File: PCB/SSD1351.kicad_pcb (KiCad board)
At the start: 2 copper layers, 38 x 41.1 mm, 20 parts, among them J1 Conn_01x07

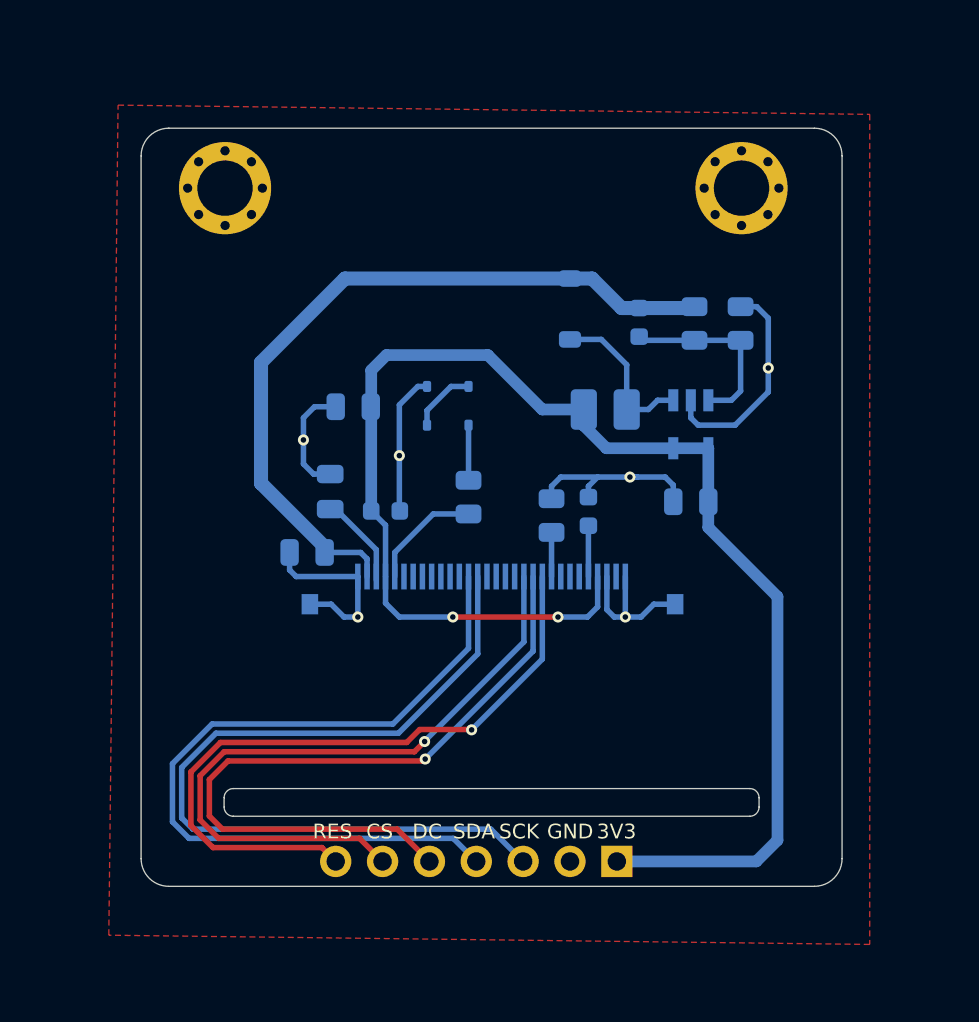
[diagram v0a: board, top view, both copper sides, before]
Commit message: Updated PCB
Consulted datasheets and adjusted cap ratings.
Reworked power distribution and location.
Started tracking down specific components and updating the BOM.
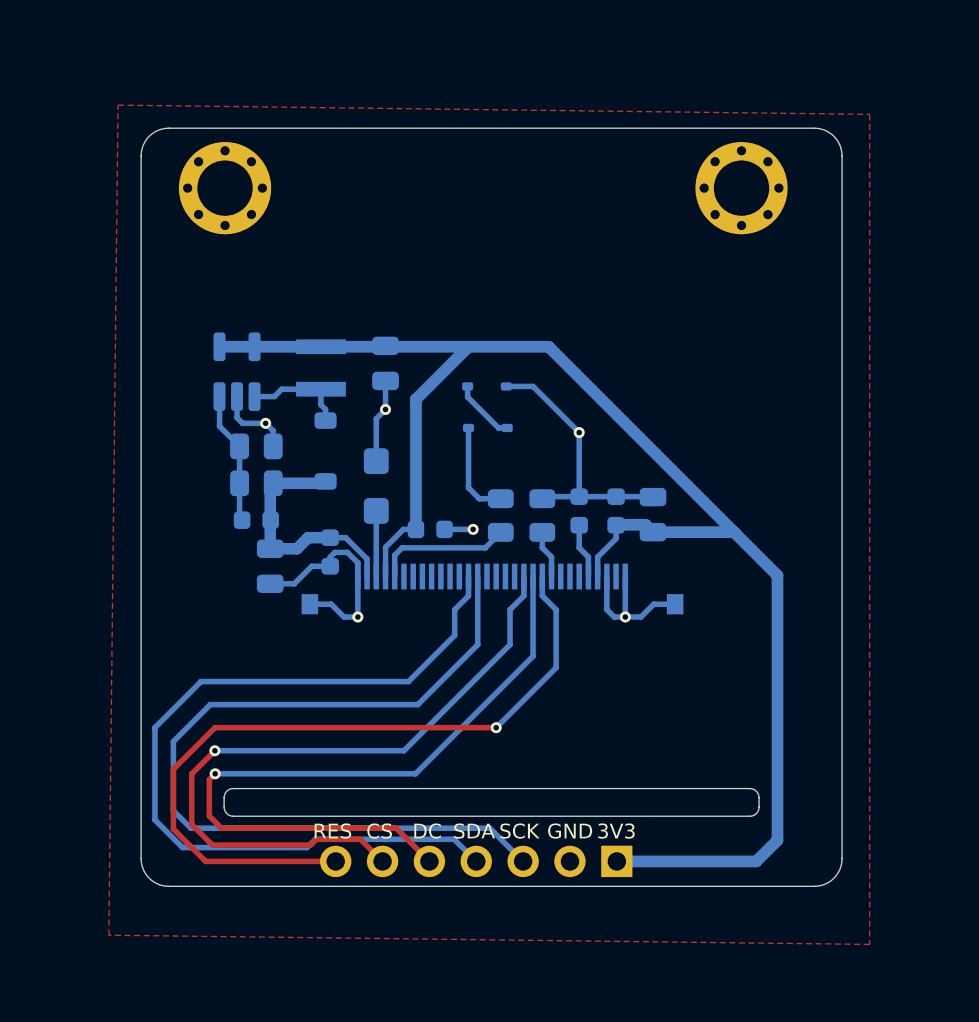
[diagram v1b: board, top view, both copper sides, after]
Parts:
- added C8: 0.1uF, Capacitor_SMD:C_0603_1608Metric, B.Cu at (128.2, 56.8)
- added C9: 0.1uF, Capacitor_SMD:C_0603_1608Metric, B.Cu at (112.8, 59.0)
- C1: value 10uf -> 10uF
- C2: value 10uF -> 4.7uF 25v Tantalum; footprint Capacitor_SMD:C_0805_2012Metric -> Capacitor_Tantalum_SMD:CP_EIA-3216-18_Kemet-A
- C5, C7: value 10uF -> 4.7uF
- C6: value 0.1uF -> 140pF
- D1, D2: value 1N4148 -> 1N4148 0.5W
- L1: value 10uH -> LVS303012H-100M-N; footprint Inductor_SMD:L_1008_2520Metric_Pad1.43x2.20mm_HandSolder -> Inductor_SMD:L_Sunlord_SWPA3012S
- R1: value 50 -> 50 1/4W
- R2: value 600K -> 560K
- R3: value 100K -> 137K
- R4: value 10K -> 14.3K
- U1: value ~ -> SFV30R-4STBE1HLF
- U2: value ~ -> FAN5331SXCT-ND; footprint SSD1351:SOT23-5 -> Package_TO_SOT_SMD:SOT-23-5_HandSoldering
- moved R4 27.1 mm to (108.8, 53.2), turned to 180 degrees
- moved R3 25.3 mm to (108.8, 55.2), turned to 0 degrees
- moved U2 24.8 mm to (107.7, 49.2), turned to 90 degrees
- moved C6 23.4 mm to (108.8, 57.2), turned to 180 degrees
- moved C7 18.2 mm to (115.8, 48.8), turned to -90 degrees
- moved C5 17.3 mm to (130.2, 57.0), turned to 90 degrees
- moved L1 15.6 mm to (112.2, 49.0), turned to -90 degrees
- moved D3 15.3 mm to (112.5, 53.5), turned to 90 degrees
- moved D2 3.42 mm to (121.2, 50.0), turned to 180 degrees
- moved C3 2.62 mm to (118.2, 57.8)
- moved C2 2.52 mm to (115.2, 55.4)
- moved C1 2.14 mm to (109.5, 59.8), turned to 90 degrees
- moved R1 2.02 mm to (122.0, 57.0)
- moved D1 1.59 mm to (121.3, 52.2), turned to 180 degrees
- moved C4 0.50 mm to (126.2, 56.8)
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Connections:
- C1 pad 1: /+13V -> GND
- C1 pad 2: GND -> /+13V
- REF** pad 1: (no net) -> GND (x2)
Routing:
- net /+13V: track 41.2 -> 13.3 mm
- net GND: track 54.8 -> 44.4 mm
- net /+3V3: track 79.8 -> 83.4 mm, vias 2 -> 0
- net /RES#: track 37.6 -> 41.1 mm
- net Net-(D3-A): track 8.80 -> 5.57 mm
- net Net-(U2-FB): track 10.3 -> 7.21 mm
- net /D1/MOSI: track 43.0 -> 45.6 mm
- net Net-(D1-A): track 2.99 -> 5.24 mm
- net Net-(C2-P$1): track 5.06 -> 3.71 mm
- net Net-(U1-VSL): track 6.17 -> 7.42 mm
- net /DO/SCK: track 45.0 -> 46.2 mm
- net /CS#: track 37.3 -> 38.3 mm

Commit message: Adding datasheets and more pcb design changes
* Added datasheets for ICs
* Removed unused footprints
* Updated PCB to use correct sized caps
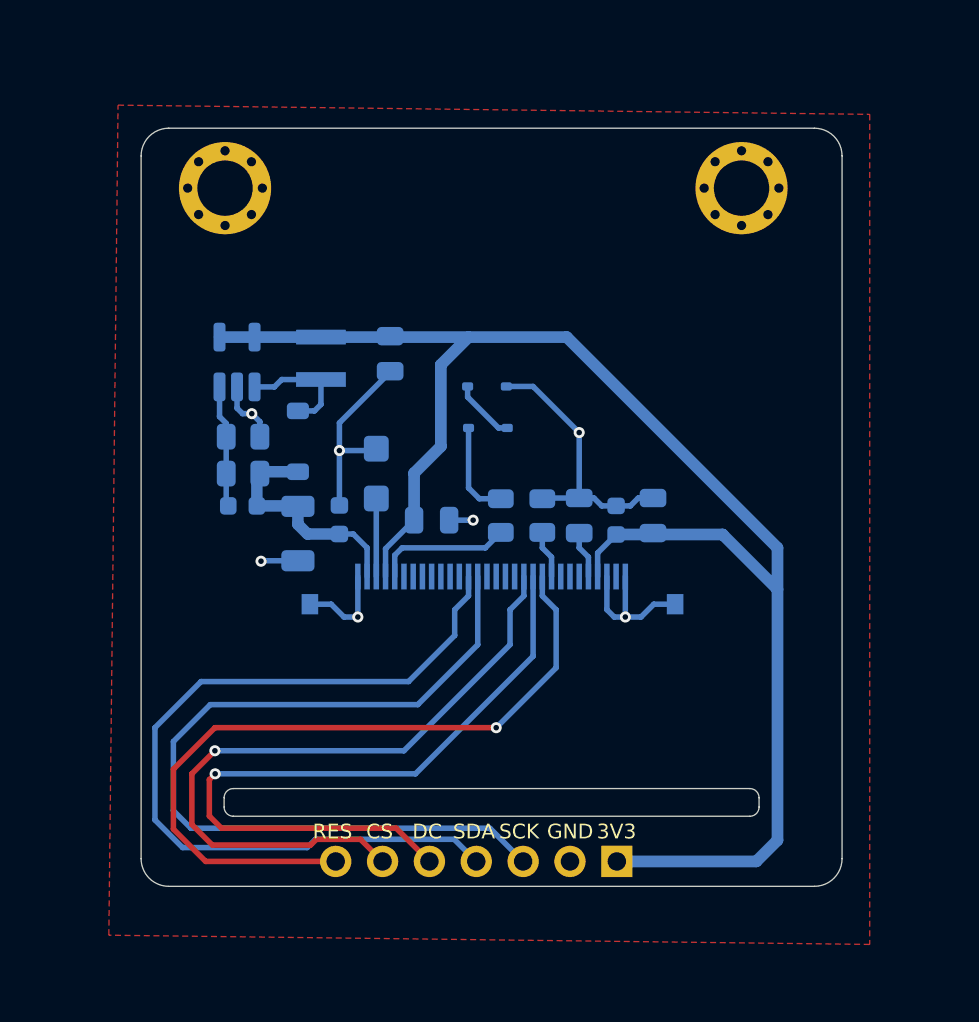
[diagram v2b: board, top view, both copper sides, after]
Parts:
- removed the C1 at (109.5, 59.8)
- added C3: 10uF, Capacitor_SMD:C_1206_3216Metric, B.Cu at (111.0, 58.0)
- C2: renamed from C6; value 140pF -> 0603B151K500NT
- C5: renamed from C2; value 4.7uF 25v Tantalum -> TC212A475K025Y
- C6: renamed from C3; footprint Capacitor_SMD:C_0603_1608Metric -> Capacitor_SMD:C_0805_2012Metric
- C7: renamed from C4; footprint Capacitor_SMD:C_0603_1608Metric -> Capacitor_SMD:C_0805_2012Metric
- moved C4 1.82 mm to (113.2, 57.2), turned to -90 degrees
- moved D3 1.59 mm to (111.0, 53.0)
- moved C2 1.08 mm to (108.0, 56.5)
- moved R3 0.90 mm to (108.0, 54.7)
- moved R4 0.90 mm to (108.0, 52.7)
- moved C5 0.67 mm to (115.2, 54.7)
- moved C1 0.58 mm to (116.0, 48.2)
- moved L1 0.52 mm to (112.2, 48.5)
- moved U2 0.52 mm to (107.7, 48.7)
- moved C6 0.51 mm to (118.2, 57.2)
- moved C8 0.50 mm to (128.2, 57.2)
- moved C7 0.25 mm to (126.2, 57.0)
- renumbered C7 to C1, C9 to C4, C5 to C9
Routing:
- net /+3V3: track 83.4 -> 87.5 mm
- net GND: track 44.4 -> 45.4 mm, vias 6 -> 7
- net Net-(D3-A): track 5.57 -> 6.51 mm
- net Net-(U2-FB): track 7.21 -> 6.65 mm
- net Net-(C5-P$1): track 3.71 -> 4.23 mm

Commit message: Changing 13v boost converter
Replace the FAN5331 with MIC2288 as a result of some sourcing issues. Redesigned and updated all the relevant components.

Added in some new footprints to make hand soldering easier for inductor and boost converter.
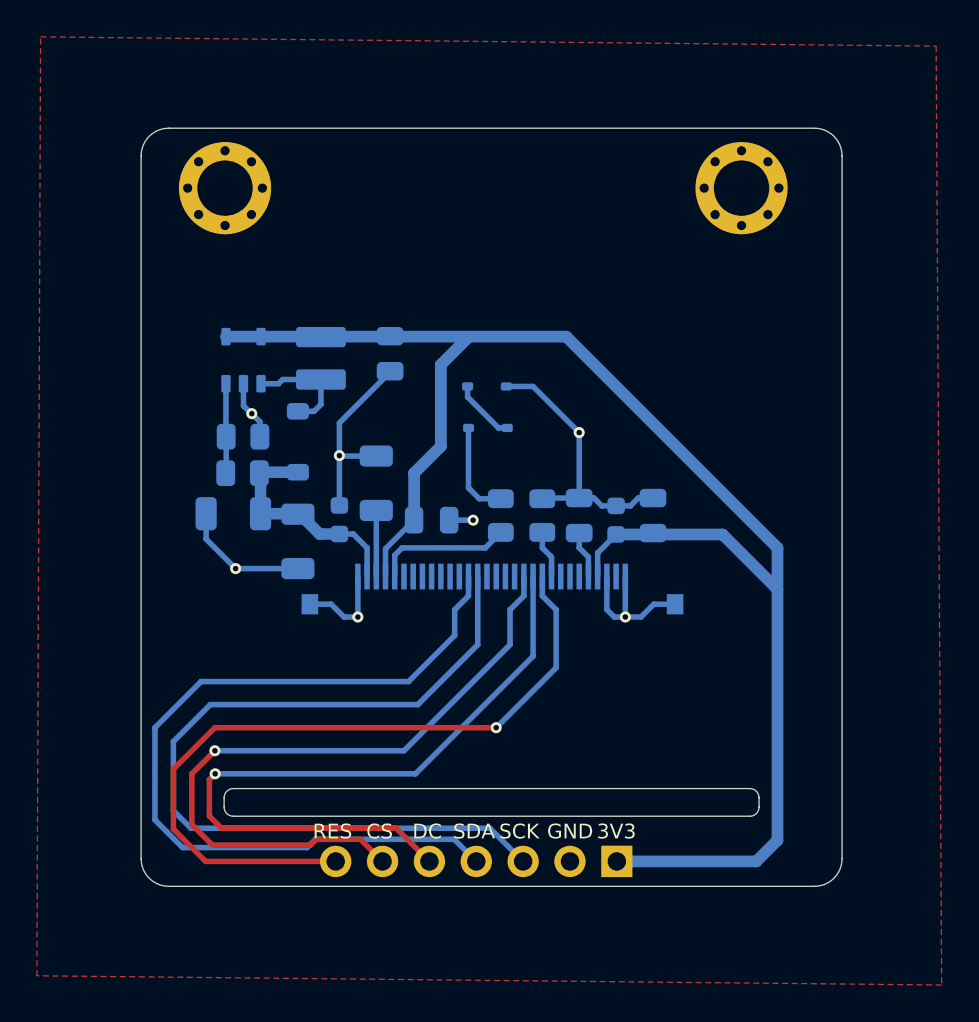
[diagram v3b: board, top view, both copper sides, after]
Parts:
- C1: value 4.7uF -> 2.2uF
- C2: value 0603B151K500NT -> 4.7uF; footprint Capacitor_SMD:C_0603_1608Metric -> Capacitor_SMD:C_1206_3216Metric
- C3: value 10uF -> 4.7uF
- C5: value TC212A475K025Y -> 4.7uF; footprint Capacitor_Tantalum_SMD:CP_EIA-3216-18_Kemet-A -> Capacitor_SMD:C_1206_3216Metric
- D1, D2: value 1N4148 0.5W -> 1N4148
- D3: value BAT54T1G -> MBR130T1G
- L1: value LVS303012H-100M-N -> LQH3NPH100MMEL; footprint Inductor_SMD:L_Sunlord_SWPA3012S -> SSD1351:IND_LQH3NPH100MMEL
- R1: value 50 1/4W -> 50
- R3: value 137K -> 30K
- R4: value 14.3K -> 3.16K
- U2: value FAN5331SXCT-ND -> MIC2288YD5-TR; footprint Package_TO_SOT_SMD:SOT-23-5_HandSoldering -> SSD1351:TSOT-23-5_D5_MCH
- moved C2 0.66 mm to (107.5, 56.9)
- moved C5 0.52 mm to (115.2, 55.2)
- moved C3 0.42 mm to (111.0, 58.4)
- moved U2 0.36 mm to (108.1, 48.6)
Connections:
- C2 pad 2: Net-(U2-FB) -> GND
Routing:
- net GND: track 45.4 -> 50.1 mm
- net Net-(U2-FB): track 6.65 -> 4.86 mm
- net /+13V: track 13.0 -> 12.3 mm
- net Net-(C5-P$1): track 4.23 -> 3.58 mm

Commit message: More power system changes
Swapping out MLC2288 for TLV61046A and removing redundant diode.

Also swapped out inductor for a more efficient one.
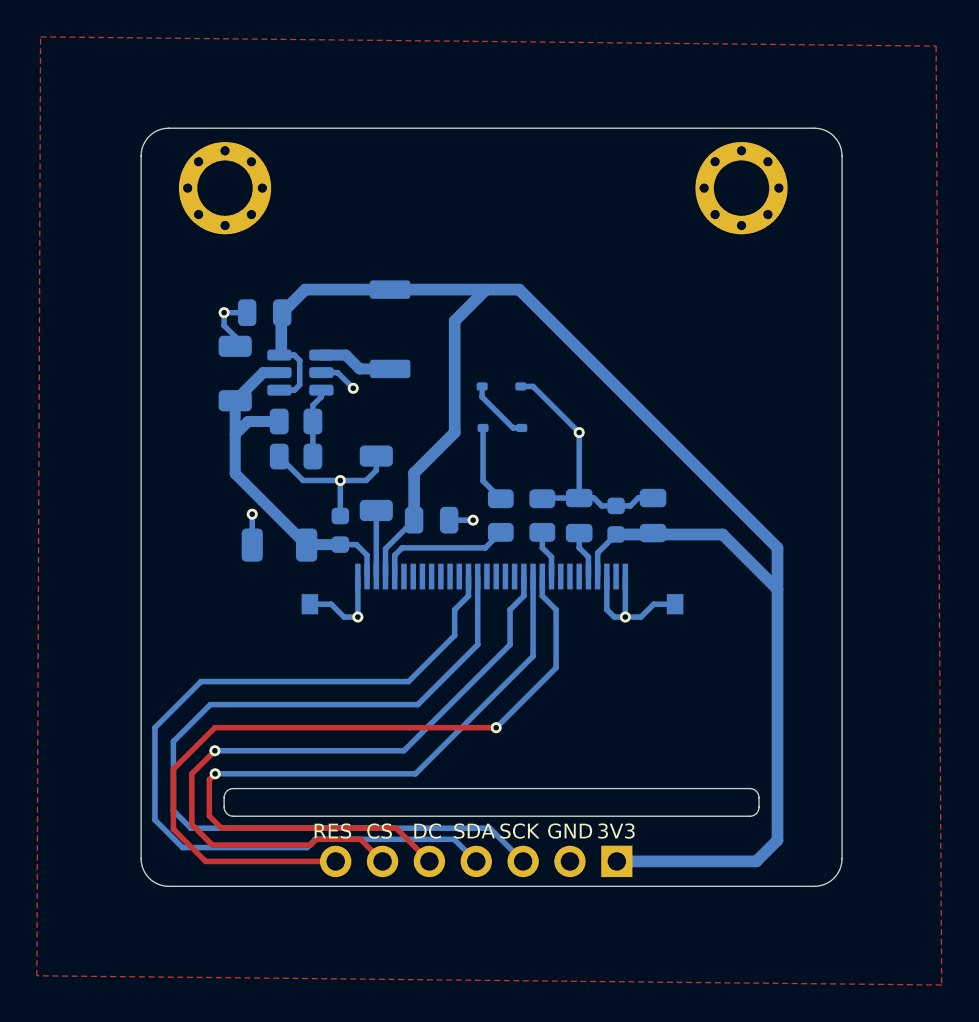
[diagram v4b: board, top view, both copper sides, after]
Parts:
- removed D3: MBR130T1G, Diode_SMD:D_SOD-123
- C1: value 2.2uF -> 4.7uF
- L1: value LQH3NPH100MMEL -> 1235AS-H-100M=P3; footprint SSD1351:IND_LQH3NPH100MMEL -> SSD1351:IND_1235AS-H-100M=P3
- R1: value 50 -> CRCW080550R0FKTA
- R2: value 560K -> ERJ-PB6B5623V
- R3: value 30K -> 806K
- R4: value 3.16K -> 52.3K
- U2: value MIC2288YD5-TR -> TLV61046ADBVT; footprint SSD1351:TSOT-23-5_D5_MCH -> Package_TO_SOT_SMD:SOT-23-6
- moved C2 7.60 mm to (107.6, 49.3), turned to 90 degrees
- moved C1 7.15 mm to (109.2, 46.0), turned to 180 degrees
- moved L1 4.07 mm to (116.0, 46.9)
- moved R3 4.03 mm to (110.9, 51.9), turned to 180 degrees
- moved U2 3.16 mm to (111.1, 49.2), turned to 180 degrees
- moved R4 3.07 mm to (110.9, 53.8), turned to 0 degrees
- moved C3 1.02 mm to (110.0, 58.6), turned to 0 degrees
- moved D1 0.79 mm to (122.1, 52.2)
- moved D2 0.79 mm to (122.0, 50.0)
- moved C4 0.58 mm to (113.3, 57.8)
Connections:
- U2 pad 5: /+3V3 -> /+13V
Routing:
- net /+13V: track 12.3 -> 19.8 mm
- net /+3V3: track 87.2 -> 94.7 mm
- net GND: track 50.1 -> 44.4 mm, vias 7 -> 8
- net Net-(U2-SW): track 6.10 -> 4.04 mm
- net Net-(U2-FB): track 4.86 -> 3.79 mm
- net Net-(D1-A): track 5.24 -> 4.24 mm
